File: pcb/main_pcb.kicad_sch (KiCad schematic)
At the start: 34 parts, among them J1 Conn_01x06_Socket, J2 Conn_01x10_Pin, J3 Conn_01x06_Pin, J4 USB_C_Receptacle_USB2.0, Q1 Si2323DS, SW1 SW_Push, SW2 SW_Push, SW3 SW_Push, U1 ESP32-H2-MINI-1, U2 LM5165Y

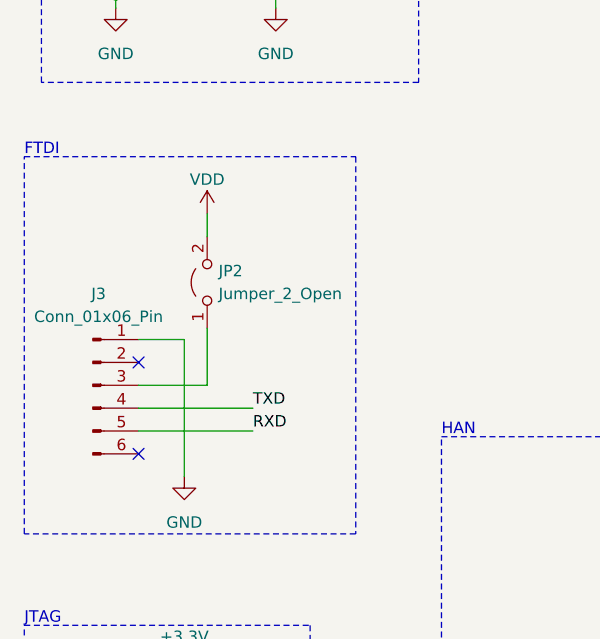
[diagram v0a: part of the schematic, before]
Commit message: Replace FTDI power pin jumper with solder bridge
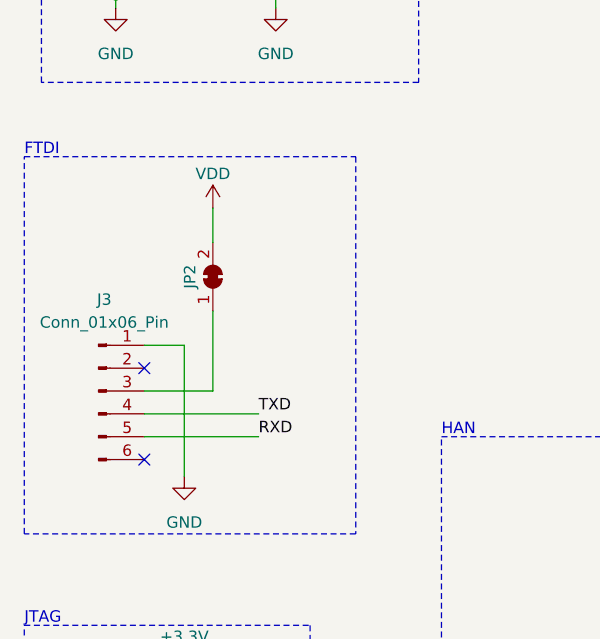
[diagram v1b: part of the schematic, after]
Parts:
- removed JP2: Jumper_2_Open, Connector_PinHeader_2.54mm:PinHeader_1x02_P2.54mm_Horizontal, symbol Jumper:Jumper_2_Open
- added JP2: SolderJumper_2_Bridged, Jumper:SolderJumper-2_P1.3mm_Open_TrianglePad1.0x1.5mm, symbol Jumper:SolderJumper_2_Bridged
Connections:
- net VDD: now also JP2.2 (B)
- net at J3.3 (Pin_3): now also JP2.1 (A)
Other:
- moved on the sheet: J3
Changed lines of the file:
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@@
   (no_connect (at 29.845 259.715))
   (no_connect (at 82.55 251.46))
-  (no_connect (at 32.385 193.675))
-  (no_connect (at 32.385 203.835))
+  (no_connect (at 33.02 194.31))
+  (no_connect (at 33.02 204.47))
   (no_connect (at 48.26 91.44))
   (no_connect (at 48.26 93.98))
@@
     (stroke (width 0) (type default))
   )
-  (wire (pts (xy 32.385 201.295) (xy 45.085 201.295))
+  (wire (pts (xy 40.64 196.85) (xy 40.64 187.96))
     (stroke (width 0) (type default))
   )
@@
     (stroke (width 0) (type default))
   )
+  (wire (pts (xy 33.02 199.39) (xy 45.72 199.39))
+    (stroke (width 0) (type default))
+  )
   (wire (pts (xy 33.02 101.6) (xy 33.02 103.505))
     (stroke (width 0) (type default))
@@
     (stroke (width 0) (type default))
   )
+  (wire (pts (xy 33.02 201.93) (xy 45.72 201.93))
+    (stroke (width 0) (type default))
+  )
   (wire (pts (xy 216.535 93.345) (xy 216.535 93.98))
     (stroke (width 0) (type default))
@@
     (stroke (width 0) (type default))
   )
-  (wire (pts (xy 40.005 196.215) (xy 40.005 189.865))
-    (stroke (width 0) (type default))
-  )
   (wire (pts (xy 142.875 182.88) (xy 147.955 182.88))
     (stroke (width 0) (type default))
@@
     (stroke (width 0) (type default))
   )
+  (wire (pts (xy 33.02 196.85) (xy 40.64 196.85))
+    (stroke (width 0) (type default))
+  )
   (wire (pts (xy 162.56 40.64) (xy 167.64 40.64))
     (stroke (width 0) (type default))
   )
-  (wire (pts (xy 32.385 191.135) (xy 37.465 191.135))
+  (wire (pts (xy 33.02 191.77) (xy 37.465 191.77))
     (stroke (width 0) (type default))
   )
@@
     (stroke (width 0) (type default))
   )
-  (wire (pts (xy 32.385 196.215) (xy 40.005 196.215))
-    (stroke (width 0) (type default))
-  )
-  (wire (pts (xy 40.005 177.165) (xy 40.005 179.705))
+  (wire (pts (xy 40.64 176.53) (xy 40.64 180.34))
     (stroke (width 0) (type default))
   )
@@
     (stroke (width 0) (type default))
   )
-  (wire (pts (xy 37.465 191.135) (xy 37.465 206.375))
+  (wire (pts (xy 37.465 191.77) (xy 37.465 206.375))
     (stroke (width 0) (type default))
   )
@@
   )
   (wire (pts (xy 220.345 196.85) (xy 220.345 199.39))
-    (stroke (width 0) (type default))
-  )
-  (wire (pts (xy 32.385 198.755) (xy 45.085 198.755))
     (stroke (width 0) (type default))
   )
@@
     (effects (font (size 1.27 1.27)) (justify left bottom))
   )
-  (label "RXD" (at 45.085 201.295 0) (fields_autoplaced)
+  (label "RXD" (at 45.72 201.93 0) (fields_autoplaced)
     (effects (font (size 1.27 1.27)) (justify left bottom))
   )
@@
     (effects (font (size 1.27 1.27)) (justify left bottom))
   )
-  (label "TXD" (at 45.085 198.755 0) (fields_autoplaced)
+  (label "TXD" (at 45.72 199.39 0) (fields_autoplaced)
     (effects (font (size 1.27 1.27)) (justify left bottom))
   )
@@
     )
   )
-  (symbol (lib_id "Jumper:Jumper_2_Open") (at 40.005 184.785 90) (unit 1)
-    (in_bom yes) (on_board yes) (dnp no) (fields_autoplaced)
-    (property "Reference" "JP2" (at 41.275 183.515 90)
-      (effects (font (size 1.27 1.27)) (justify right))
-    )
-    (property "Value" "Jumper_2_Open" (at 41.275 186.055 90)
-      (effects (font (size 1.27 1.27)) (justify right))
-    )
-    (property "Footprint" "Connector_PinHeader_2.54mm:PinHeader_1x02_P2.54mm_Horizontal" (at 40.005 184.785 0)
-      (effects (font (size 1.27 1.27)) hide)
-    )
-    (property "Datasheet" "~" (at 40.005 184.785 0)
-      (effects (font (size 1.27 1.27)) hide)
-    )
-    (pin "2")
-    (pin "1")
-    (instances
-      (project "main_pcb"
-        (path "/6204b7c2-8814-41ee-9243-5078f55f08d4"
-          (reference "JP2") (unit 1)
-        )
-      )
-    )
-  )
   (symbol (lib_id "Device:R") (at 60.96 73.66 90) (unit 1)
     (in_bom yes) (on_board yes) (dnp no)
@@
     )
   )
-  (symbol (lib_id "power:VDD") (at 40.005 177.165 0) (unit 1)
+  (symbol (lib_id "power:VDD") (at 40.64 176.53 0) (unit 1)
     (in_bom yes) (on_board yes) (dnp no)
-    (property "Reference" "#PWR020" (at 40.005 180.975 0)
-      (effects (font (size 1.27 1.27)) hide)
-    )
-    (property "Value" "VDD" (at 40.005 173.355 0)
-      (effects (font (size 1.27 1.27)))
-    )
-    (property "Footprint" "" (at 40.005 177.165 0)
-      (effects (font (size 1.27 1.27)) hide)
-    )
-    (property "Datasheet" "" (at 40.005 177.165 0)
+    (property "Reference" "#PWR020" (at 40.64 180.34 0)
+      (effects (font (size 1.27 1.27)) hide)
+    )
+    (property "Value" "VDD" (at 40.64 172.72 0)
+      (effects (font (size 1.27 1.27)))
+    )
+    (property "Footprint" "" (at 40.64 176.53 0)
+      (effects (font (size 1.27 1.27)) hide)
+    )
+    (property "Datasheet" "" (at 40.64 176.53 0)
       (effects (font (size 1.27 1.27)) hide)
     )
@@
     )
   )
+  (symbol (lib_id "Jumper:SolderJumper_2_Bridged") (at 40.64 184.15 90) (unit 1)
+    (in_bom yes) (on_board yes) (dnp no)
+    (property "Reference" "JP2" (at 38.1 184.15 0)
+      (effects (font (size 1.27 1.27)))
+    )
+    (property "Value" "SolderJumper_2_Bridged" (at 44.45 184.15 0)
+      (effects (font (size 1.27 1.27)) hide)
+    )
+    (property "Footprint" "Jumper:SolderJumper-2_P1.3mm_Open_TrianglePad1.0x1.5mm" (at 40.64 184.15 0)
+      (effects (font (size 1.27 1.27)) hide)
+    )
+    (property "Datasheet" "~" (at 40.64 184.15 0)
+      (effects (font (size 1.27 1.27)) hide)
+    )
+    (pin "2")
+    (pin "1")
+    (instances
+      (project "main_pcb"
+        (path "/6204b7c2-8814-41ee-9243-5078f55f08d4"
+          (reference "JP2") (unit 1)
+        )
+      )
+    )
+  )
   (symbol (lib_id "Device:R") (at 47.625 135.255 0) (unit 1)
     (in_bom yes) (on_board yes) (dnp no) (fields_autoplaced)
@@
     )
   )
-  (symbol (lib_id "Connector:Conn_01x06_Pin") (at 27.305 196.215 0) (unit 1)
-    (in_bom yes) (on_board yes) (dnp no) (fields_autoplaced)
-    (property "Reference" "J3" (at 27.94 186.055 0)
-      (effects (font (size 1.27 1.27)))
-    )
-    (property "Value" "Conn_01x06_Pin" (at 27.94 188.595 0)
-      (effects (font (size 1.27 1.27)))
-    )
-    (property "Footprint" "Connector_PinHeader_2.54mm:PinHeader_1x06_P2.54mm_Horizontal" (at 27.305 196.215 0)
-      (effects (font (size 1.27 1.27)) hide)
-    )
-    (property "Datasheet" "~" (at 27.305 196.215 0)
-      (effects (font (size 1.27 1.27)) hide)
-    )
+  (symbol (lib_id "Connector:Conn_01x06_Pin") (at 27.94 196.85 0) (unit 1)
+    (in_bom yes) (on_board yes) (dnp no) (fields_autoplaced)
+    (property "Reference" "J3" (at 28.575 186.69 0)
+      (effects (font (size 1.27 1.27)))
+    )
+    (property "Value" "Conn_01x06_Pin" (at 28.575 189.23 0)
+      (effects (font (size 1.27 1.27)))
+    )
+    (property "Footprint" "Connector_PinHeader_2.54mm:PinHeader_1x06_P2.54mm_Horizontal" (at 27.94 196.85 0)
+      (effects (font (size 1.27 1.27)) hide)
+    )
+    (property "Datasheet" "~" (at 27.94 196.85 0)
+      (effects (font (size 1.27 1.27)) hide)
+    )
